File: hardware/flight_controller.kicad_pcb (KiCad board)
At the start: 6 copper layers, 50 x 50 mm, 83 parts, among them IC2 STM32F722RET6, IC3 W25Q128JVSIQ, J2 Conn_01x08, J3 Conn_01x04, J4 Conn_01x04, J5 Conn_01x04, J6 USB4105-GF-A-060, Q1 TPRT9013-33GB, SW2 SW_SPST, U1 BMP581, U2 MP9943GQ-Z, U3 USBLC6-2P6, U4 MP9943GQ-Z, Y1 Q13FC13500004, Y2 X322525MOB4SI

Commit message: layout
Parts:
- moved R15 1.10 mm to (190.6, 110.3), turned to -90 degrees
- moved C1 0.81 mm to (163.6, 99.4)
- moved C2 0.81 mm to (163.6, 101.6)
- moved C3 0.81 mm to (163.6, 103.9)
- moved C4 0.81 mm to (158.9, 98.9)
- moved C6 0.81 mm to (163.6, 106.1)
- moved C7 0.81 mm to (163.6, 108.4)
- moved R3 0.81 mm to (158.5, 97.8)
- moved C5 0.81 mm to (156.1, 102.2)
- moved L1 0.81 mm to (158.4, 105.3)
- moved R5 0.81 mm to (156.4, 101.2)
- moved R6 0.81 mm to (154.3, 103.9)
- moved R7 0.81 mm to (154.3, 105.8)
- moved R8 0.81 mm to (154.3, 104.8)
- moved U2 0.81 mm to (159.3, 101.6)
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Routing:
- net /ICM_SDO: track 0.00 -> 25.7 mm, vias 0 -> 2
- net /ICM_SDI: track 0.00 -> 23.4 mm
- net /ICM_INT1: track 0.00 -> 21.7 mm, vias 0 -> 2
- net /ICM_INT2: track 0.00 -> 18.4 mm, vias 0 -> 2
- net /ICM_CS: track 0.00 -> 10.7 mm, vias 0 -> 2
- net /ICM_SCLK: track 0.00 -> 10.5 mm
- net +3.3V: track 18.0 -> 17.3 mm
- net GNDREF: track 2.05 -> 1.91 mm, vias 8 -> 32

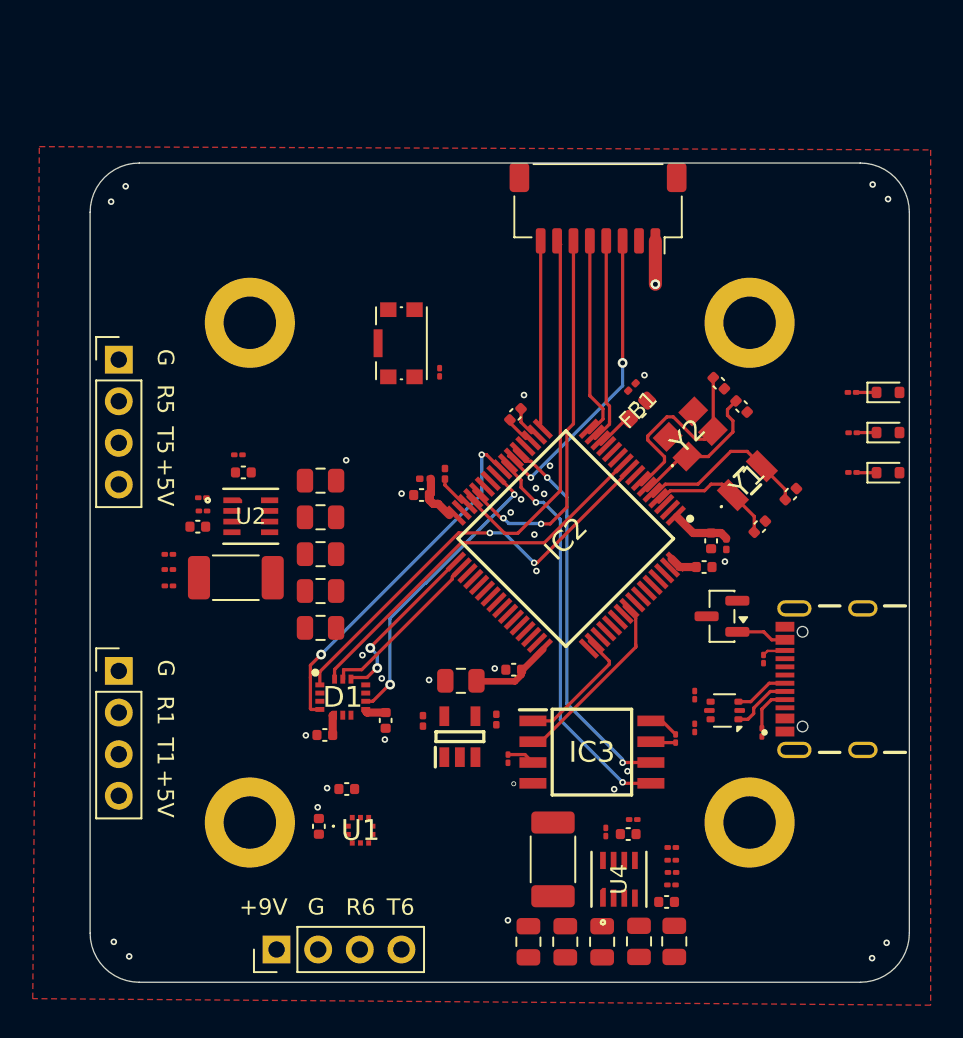
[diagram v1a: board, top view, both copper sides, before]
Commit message: redefined signal layout
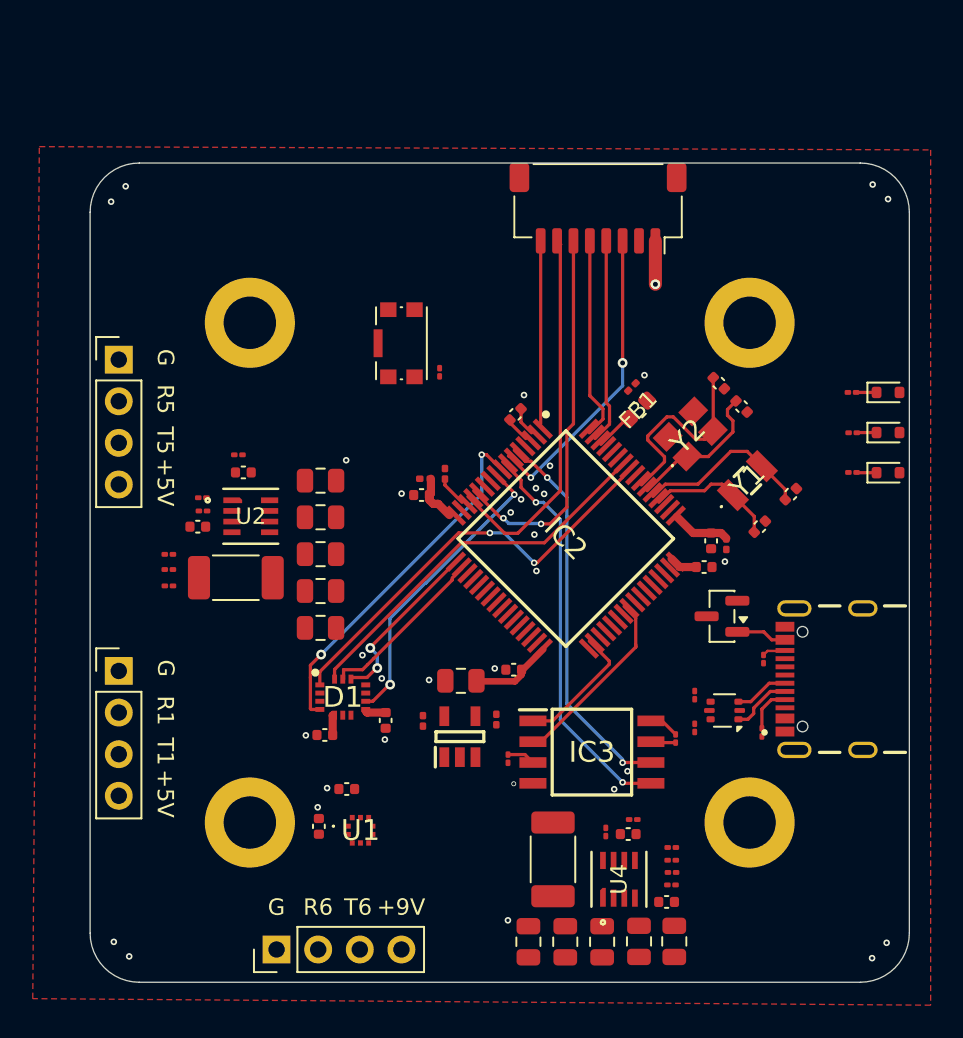
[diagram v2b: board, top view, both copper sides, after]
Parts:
- turned IC2 to -45 degrees
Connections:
- net /SPI1_MOSI renamed /FLASH_MOSI
- net /SPI1_SCLK renamed /FLASH_SCLK
- D1 pad 1: /ICM_SDO -> /ICM_MISO
- D1 pad 14: /ICM_SDI -> /ICM_MOSI
- IC2 pad 10: /ICM_SDI -> unconnected-(IC2-PC2-Pad10)
- IC2 pad 16: /USART2_TX -> /TRANSCEIVER_TX
- IC2 pad 17: /UART2_RX -> /TRANSCEIVER_RX
- IC2 pad 2: unconnected-(IC2-PC13-Pad2) -> /ANALOG_INPUT
- IC2 pad 20: unconnected-(IC2-PA4-Pad20) -> /CS_FLASH
- IC2 pad 22: /ANALOG_PIN -> /FLASH_MISO
- IC2 pad 24: /ICM_INT1 -> unconnected-(IC2-PC4-Pad24)
- IC2 pad 25: /ICM_INT2 -> unconnected-(IC2-PB0-Pad25)
- IC2 pad 27: unconnected-(IC2-PB2-Pad27) -> /BMP_INT
- IC2 pad 28: /TIM2_CH3 -> /BMP_SCLK
- IC2 pad 29: /TIM2_CH4 -> /BMP_SDI
- IC2 pad 35: unconnected-(IC2-PB14-Pad35) -> /ICM_MISO
- IC2 pad 36: unconnected-(IC2-PB15-Pad36) -> /ICM_MOSI
- IC2 pad 37: /USART6_TX -> /ICM_INT2
- IC2 pad 38: /USART6_RX -> /ICM_INT1
- IC2 pad 50: /CS_FLASH -> unconnected-(IC2-PA15-Pad50)
- IC2 pad 54: /USART5_RX -> /ESC_USART_RX
- IC2 pad 56: /SPI1_MISO -> unconnected-(IC2-PB4-Pad56)
- IC2 pad 58: unconnected-(IC2-PB6-Pad58) -> /TIM4_CH1
- IC2 pad 59: /BMP_INT -> /TIM4_CH2
- IC2 pad 61: /BMP_SCK -> /TIM4_CH3
- IC2 pad 62: /BMP_SDI -> /TIM4_CH4
- IC2 pad 9: /ICM_SDO -> unconnected-(IC2-PC1-Pad9)
- IC3 pad 2: /SPI1_MISO -> /FLASH_MISO
- J2 pad 1: VBAT -> /TIM4_CH1
- J2 pad 2: GNDREF -> /TIM4_CH2
- J2 pad 3: /ANALOG_PIN -> /TIM4_CH3
- J2 pad 4: /TIM2_CH1 -> /TIM4_CH4
- J2 pad 5: /TIM2_CH2 -> /ESC_USART_RX
- J2 pad 6: /TIM2_CH3 -> /ANALOG_INPUT
- J2 pad 7: /TIM2_CH4 -> GNDREF
- J2 pad 8: /UART2_RX -> VBAT
- J3 pad 2: /UASRT6_RX -> /USART6_RX
- J4 pad 2: /USART1_RX -> /TRANSCEIVER_RX
- J4 pad 3: /USART1_TX -> /TRANSCEIVER_TX
- U1 pad 2: /BMP_SCK -> /BMP_SCLK
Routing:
- net (no net): track 0.00 -> 79.0 mm
- net GNDREF: track 1.91 -> 37.8 mm, vias 32 -> 34
- net /ICM_SDO: track 25.7 -> 0.00 mm, vias 2 -> 0
- net unconnected-(IC2-NRST-Pad7): track 0.00 -> 24.6 mm, vias 0 -> 2
- net /FLASH_MOSI: track 24.6 -> 0.00 mm, vias 2 -> 0
- net /FLASH_SCLK: track 23.7 -> 0.00 mm, vias 2 -> 0
- net /HSE_IN: track 8.96 -> 32.7 mm, vias 0 -> 2
- net /ICM_SDI: track 23.4 -> 0.00 mm
- net /TIM2_CH3: track 23.4 -> 0.00 mm, vias 2 -> 0
- net Net-(IC2-VDDA): track 2.36 -> 25.4 mm
- net /TIM2_CH4: track 23.0 -> 0.00 mm
- net /ANALOG_PIN: track 18.7 -> 0.00 mm, vias 2 -> 0
- net /TIM2_CH1: track 12.5 -> 0.00 mm
- net +3.3V: track 17.3 -> 29.7 mm
- net /TIM2_CH2: track 12.4 -> 0.00 mm
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
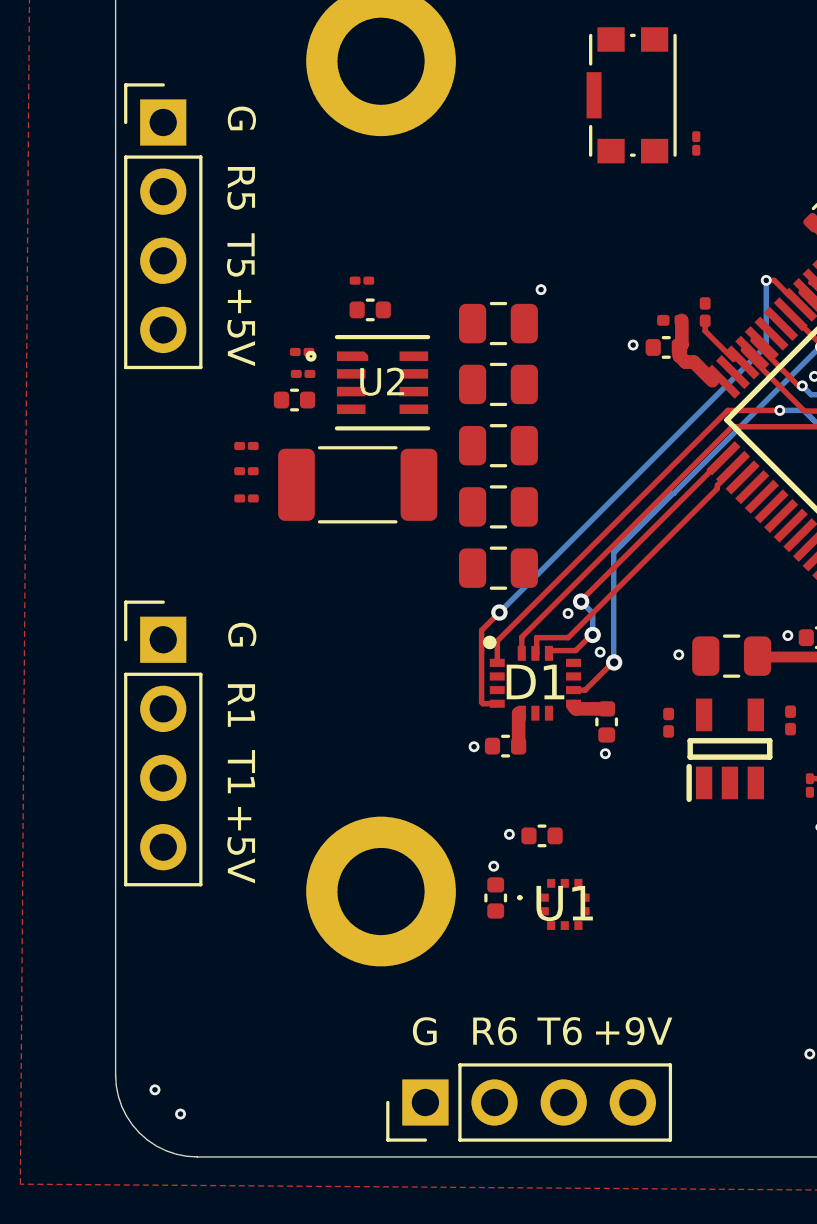
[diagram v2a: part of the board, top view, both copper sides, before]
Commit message: redefined signal layout
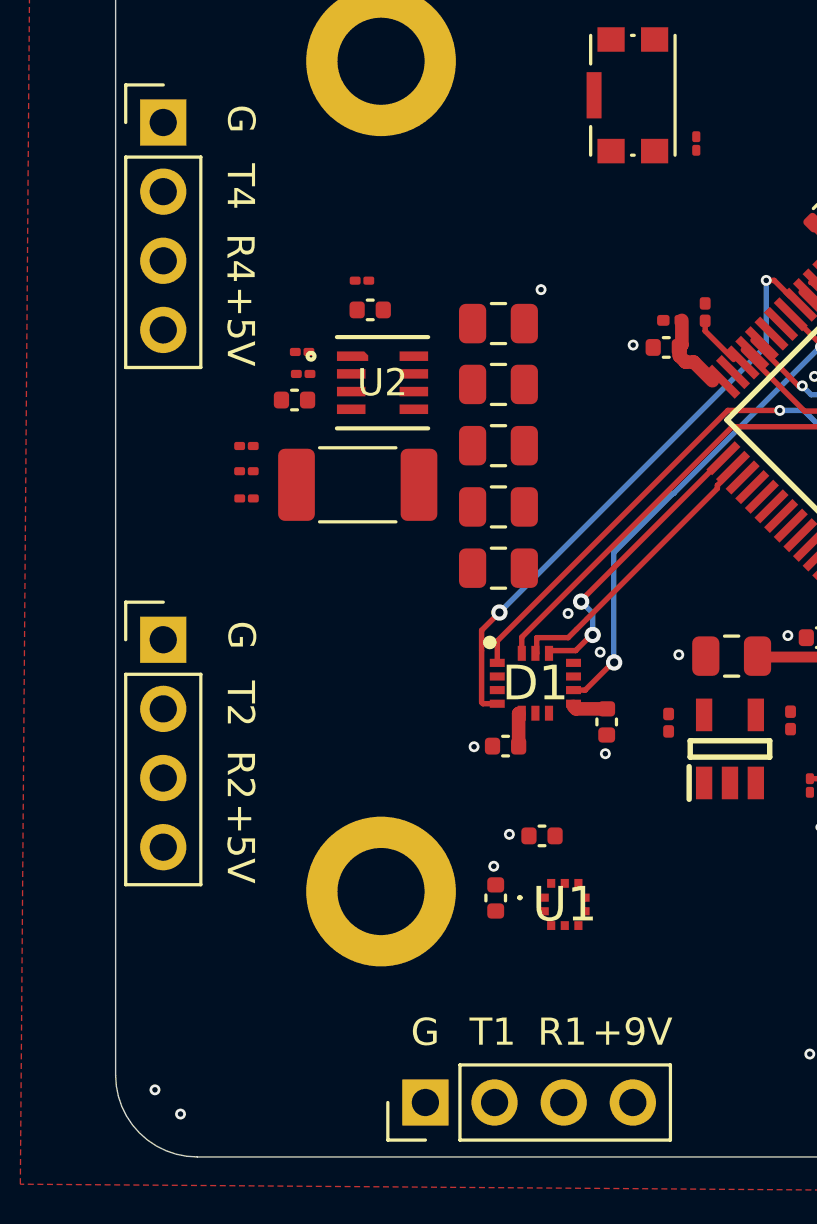
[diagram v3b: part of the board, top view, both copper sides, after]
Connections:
- IC2 pad 14: /TIM2_CH1 -> /GPS_TX
- IC2 pad 15: /TIM2_CH2 -> /GPS_RX
- IC2 pad 42: /USART1_TX -> /VTX_TX
- IC2 pad 43: /USART1_RX -> /VTX_RX
- J3 pad 2: /USART6_RX -> /VTX_TX
- J3 pad 3: /USART6_TX -> /VTX_RX
- J4 pad 2: /TRANSCEIVER_RX -> /TRANSCEIVER_TX
- J4 pad 3: /TRANSCEIVER_TX -> /TRANSCEIVER_RX
- J5 pad 2: /USART5_RX -> /GPS_TX
- J5 pad 3: /USART5_TX -> /GPS_RX
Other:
- board text added: "R2"
- board text added: "R4"
- board text added: "T2"
- board text added: "T4"
- board text removed: "R5"
- board text removed: "R6"
- board text removed: "T5"
- board text removed: "T6"

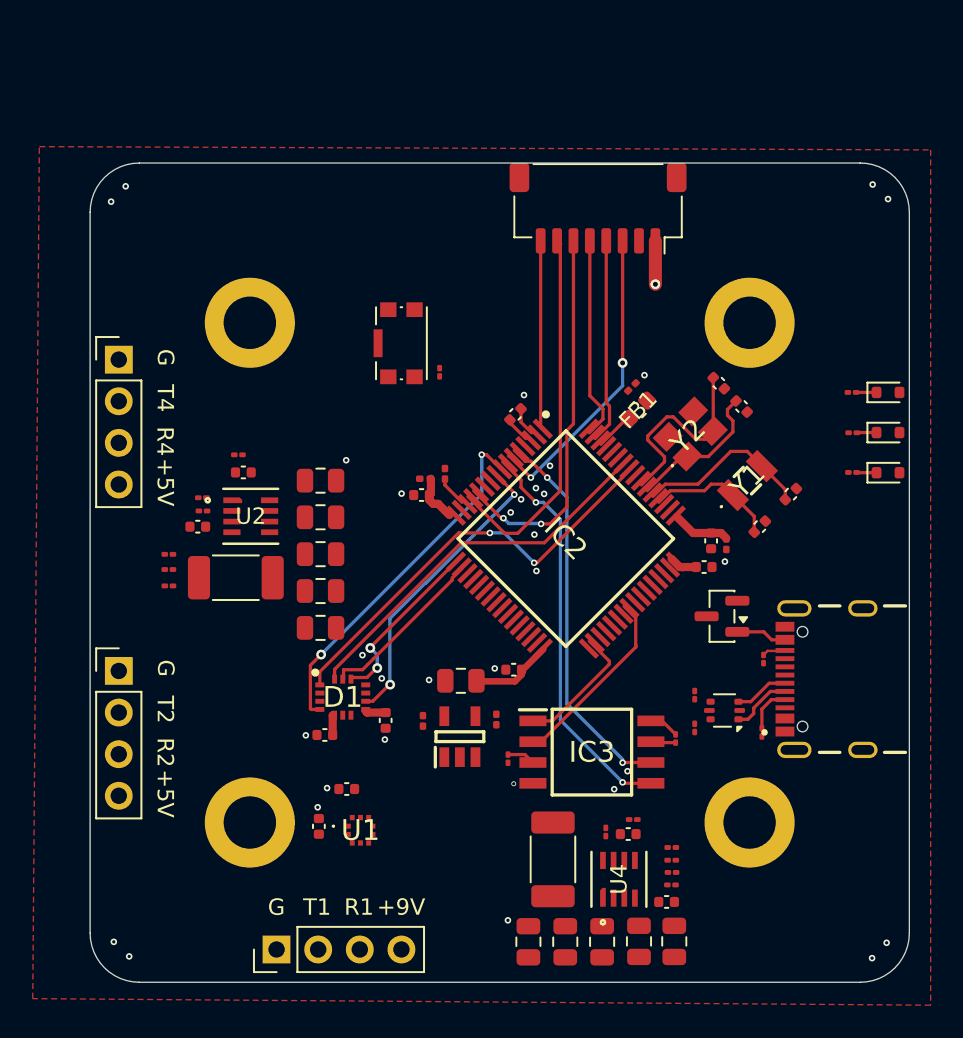
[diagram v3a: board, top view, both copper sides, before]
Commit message: redefined signal layout
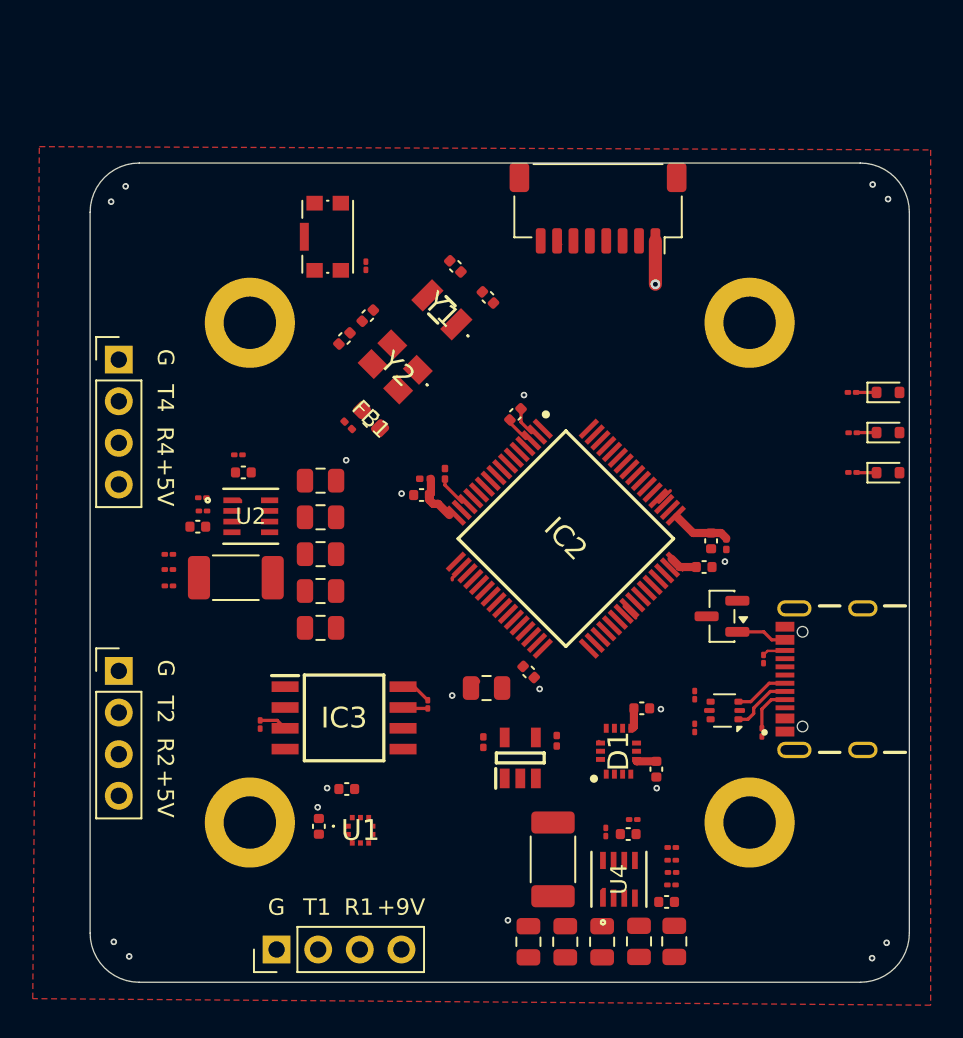
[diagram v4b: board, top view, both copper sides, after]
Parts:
- moved C34 24.7 mm to (171.8, 86.3), turned to -45 degrees
- moved C35 23.5 mm to (166.4, 89.3), turned to -135 degrees
- moved C36 23.0 mm to (165.0, 90.7), turned to -135 degrees
- moved C33 21.7 mm to (173.8, 88.2), turned to -45 degrees
- moved Y1 21.4 mm to (171.0, 89.0), turned to 135 degrees
- moved C22 20.3 mm to (184.1, 117.0), turned to -90 degrees
- moved Y2 18.5 mm to (168.1, 92.4), turned to 135 degrees
- moved C28 17.5 mm to (165.3, 96.0), turned to -45 degrees
- moved D1 17.2 mm to (181.8, 115.9), turned to 90 degrees
- moved FB1 16.3 mm to (166.6, 95.6), turned to -45 degrees
- moved C21 15.6 mm to (183.2, 113.3), turned to 0 degrees
- moved R17 15.3 mm to (159.9, 114.3)
- moved IC3 15.3 mm to (165.0, 113.9)
- moved R16 15.3 mm to (170.1, 113.0)
- moved R22 7.91 mm to (166.3, 86.3)
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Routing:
- net (no net): track 79.0 -> 0.00 mm
- net GNDREF: track 37.8 -> 3.12 mm, vias 34 -> 19
- net /HSE_IN: track 32.7 -> 0.00 mm, vias 2 -> 0
- net Net-(IC2-VDDA): track 25.4 -> 0.00 mm
- net unconnected-(IC2-NRST-Pad7): track 24.6 -> 0.00 mm, vias 2 -> 0
- net /ICM_INT1: track 21.7 -> 0.00 mm, vias 2 -> 0
- net /ICM_INT2: track 18.4 -> 0.00 mm, vias 2 -> 0
- net +3.3V: track 29.7 -> 12.2 mm
- net /HSE_OUT: track 12.5 -> 0.00 mm
- net /LSE_OUT: track 10.8 -> 0.00 mm
- net /ICM_CS: track 10.7 -> 0.14 mm, vias 2 -> 0
- net unconnected-(IC2-PC9-Pad40): track 11.6 -> 1.01 mm
- net /ICM_SCLK: track 10.5 -> 0.05 mm
- net /LSE_IN: track 8.06 -> 0.00 mm
- net /CS_FLASH: track 8.01 -> 0.00 mm
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
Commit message: redefined signal layout
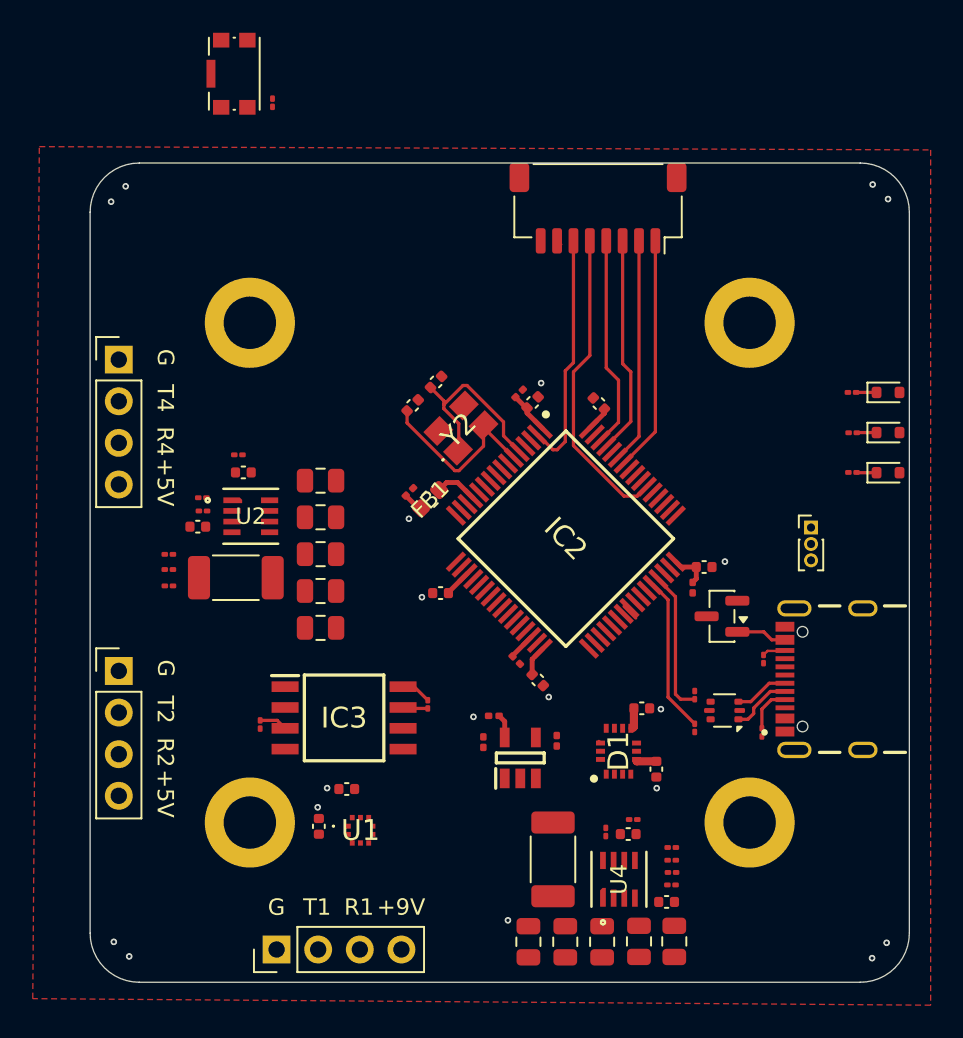
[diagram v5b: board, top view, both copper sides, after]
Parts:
- removed C33, C34: 6.8pF, Capacitor_SMD:C_0402_1005Metric
- removed Y1: Q13FC13500004, drone_footprints:Q13FC13500004
- added J1: Conn_01x03, Connector_PinHeader_1.00mm:PinHeader_1x03_P1.00mm_Vertical, F.Cu at (193.5, 102.2)
- C30: footprint Capacitor_SMD:C_0805_2012Metric -> Capacitor_SMD:C_0201_0603Metric
- moved C32 12.2 mm to (175.5, 110.3), turned to 135 degrees
- moved R22 11.5 mm to (160.6, 76.3)
- moved SW2 11.5 mm to (158.3, 74.5)
- moved C23 10.8 mm to (180.5, 94.7), turned to -45 degrees
- moved C27 7.75 mm to (175.7, 94.1), turned to -135 degrees
- moved C24 6.10 mm to (170.9, 106.2)
- moved FB1 6.07 mm to (170.2, 100.5), turned to 45 degrees
- moved C36 5.83 mm to (169.2, 94.8)
- moved C35 5.81 mm to (170.6, 93.4)
- moved C28 5.52 mm to (169.0, 100.1), turned to -135 degrees
- moved Y2 5.48 mm to (172.1, 96.2), turned to 45 degrees
- moved C29 3.35 mm to (186.3, 105.9)
- moved C30 1.75 mm to (174.1, 113.7)
- moved C31 1.27 mm to (176.5, 94.6)
- moved C25 0.74 mm to (176.8, 111.6)
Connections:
- IC2 pad 3: /LSE_IN -> unconnected-(IC2-PC14-OSC32_IN-Pad3)
- IC2 pad 4: /LSE_OUT -> unconnected-(IC2-PC15-OSC32_OUT-Pad4)
- IC2 pad 41: /STATUS -> unconnected-(IC2-PA8-Pad41)
- IC2 pad 46: unconnected-(IC2-PA13-Pad46) -> /JTAG_SWDIO
- IC2 pad 49: unconnected-(IC2-PA14-Pad49) -> /JTAG_SWCLK
- IC2 pad 50: unconnected-(IC2-PA15-Pad50) -> /STATUS
- IC2 pad 53: /USART5_TX -> unconnected-(IC2-PC12-Pad53)
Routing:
- net /ESC_USART_RX: track 0.00 -> 18.9 mm
- net /ANALOG_INPUT: track 0.00 -> 14.8 mm
- net /TIM4_CH2: track 0.00 -> 13.8 mm
- net /TIM4_CH3: track 0.00 -> 13.4 mm
- net /TIM4_CH4: track 0.00 -> 12.9 mm
- net /HSE_IN: track 0.00 -> 11.9 mm
- net /TIM4_CH1: track 2.65 -> 14.4 mm, vias 1 -> 0
- net /HSE_OUT: track 0.00 -> 11.3 mm
- net /USB_DN: track 3.74 -> 13.3 mm
- net /USB_DP: track 3.30 -> 12.1 mm
- net +3.3V: track 12.2 -> 15.4 mm
- net GNDREF: track 3.12 -> 0.40 mm
- net Net-(IC2-VDDA): track 0.00 -> 2.67 mm
- net unconnected-(IC2-PC11-Pad52): track 1.00 -> 0.00 mm
